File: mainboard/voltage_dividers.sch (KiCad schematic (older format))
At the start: 56 parts

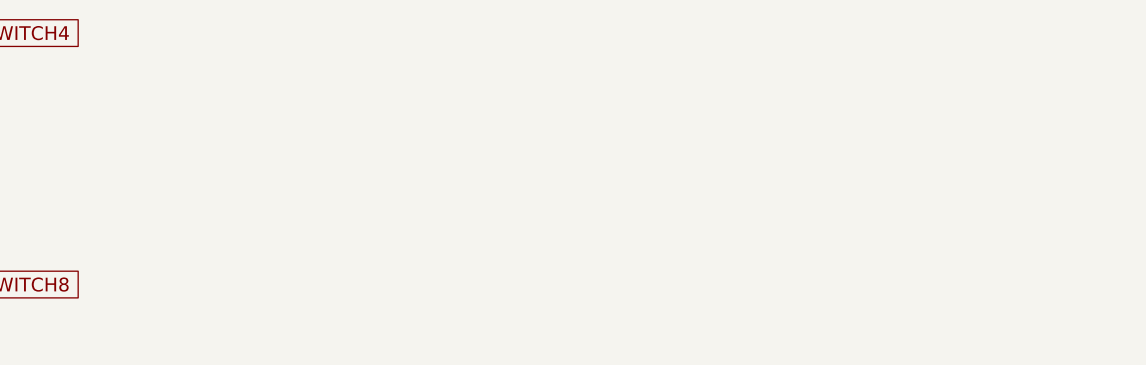
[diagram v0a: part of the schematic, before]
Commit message: Remove 5V regulator. Power directly from MOLEX connector instead. Add CC-BY-SA license.
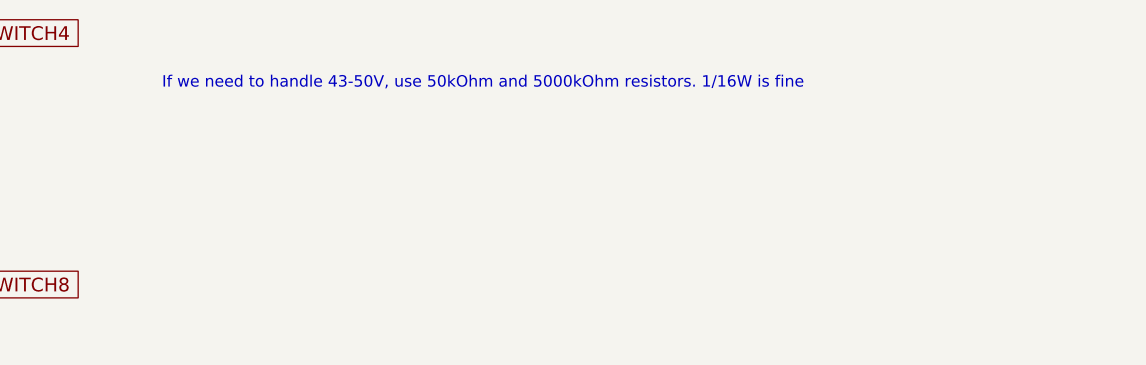
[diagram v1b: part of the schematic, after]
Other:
- note added: "If we need to handle 43-50V, use 50kOhm and 5000kOhm resistors. 1/16W is fine"
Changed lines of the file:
@@
 Text GLabel 9350 4850 0    60   Input ~ 0
 SCORE_ZERO4
+Text Notes 6300 1050 0    50   ~ 0
+If we need to handle 43-50V, use 50kOhm and 5000kOhm resistors. 1/16W is fine
 $EndSCHEMATC
